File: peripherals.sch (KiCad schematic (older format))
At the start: 23 parts, among them IC5 ATECC608A-TNGLORAU-B, J4 Conn_Coaxial, SW1 KMR221NGLFS, SW2 KMR221NGLFS, U3 MAX-8Q, U4 BAT-HLD-001

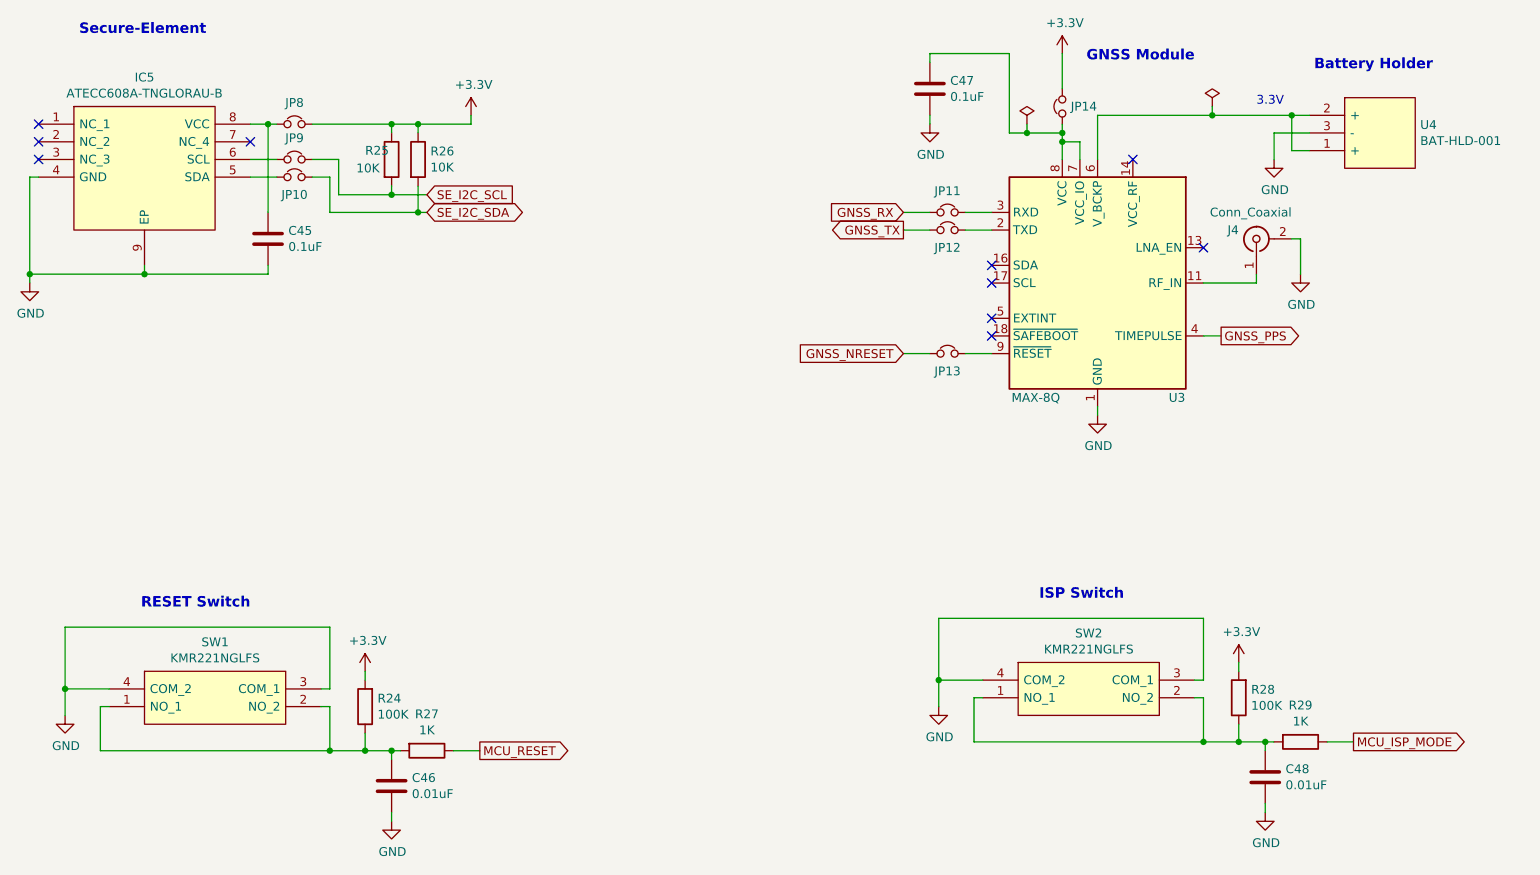
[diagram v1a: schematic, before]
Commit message: Removed jumpers from peripherals
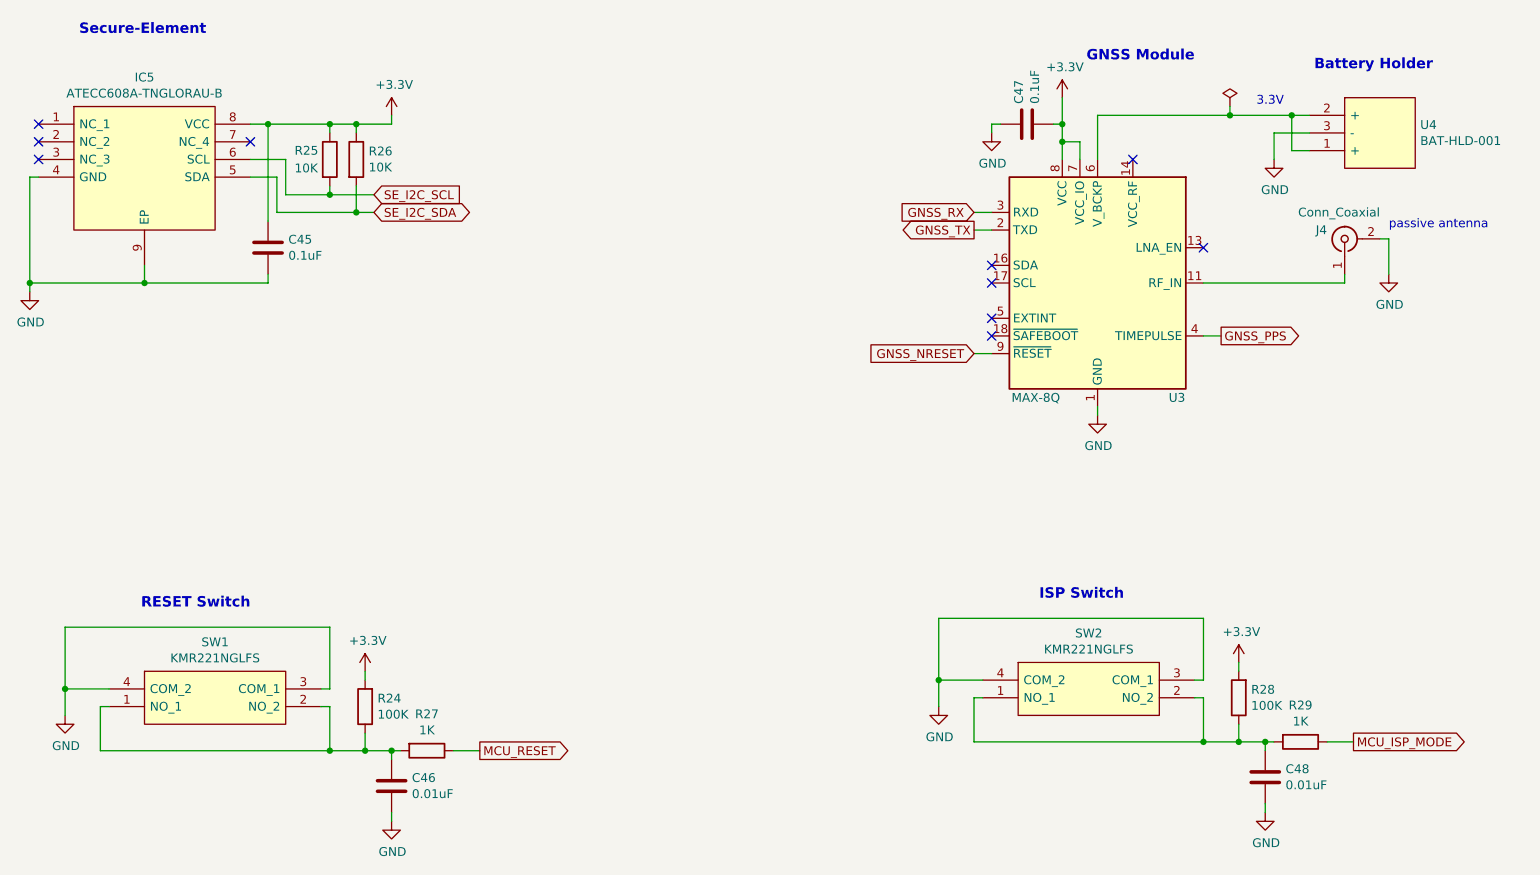
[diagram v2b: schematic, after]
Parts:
- removed JP10, JP11, JP12, JP13, JP14, JP8, JP9: Jumper_NC_Small, Jumper:SolderJumper-2_P1.3mm_Bridged_Pad1.0x1.5mm, symbol Device:Jumper_NC_Small
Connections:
- net +3V3: now also C45.1, C47.2, IC5.8 (VCC), U3.7 (VCC_IO), U3.8 (VCC)
- net GND: now also C47.1; no longer C47.2
- net GNSS_NRESET: now also U3.9 (~RESET)
- net GNSS_RX: now also U3.3 (RXD)
- net GNSS_TX: now also U3.2 (TXD)
- net SE_I2C_SCL: now also IC5.6 (SCL)
- net SE_I2C_SDA: now also IC5.5 (SDA)
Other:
- note added: "passive antenna"
- moved on the sheet: C45, C47, J4, R25, R26

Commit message: Changed all symbols names from IC to U
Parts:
- renumbered IC5 to U
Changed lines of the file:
@@
 P 2050 1900
 AR Path="/5F708DEE" Ref="IC?"  Part="1"
-AR Path="/5F708A6A/5F708DEE" Ref="IC5"  Part="1"
-F 0 "IC5" H 2650 2165 50  0000 C CNN
+AR Path="/5F708A6A/5F708DEE" Ref="U"  Part="1"
+F 0 "U" H 2650 2165 50  0000 C CNN
 F 1 "ATECC608A-TNGLORAU-B" H 2650 2074 50  0000 C CNN
 F 2 "tardigrade-components:SON50P300X200X60-9N" H 3100 2000 50  0001 L CNN

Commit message: Unnecessary note removed
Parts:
- renumbered U to U9
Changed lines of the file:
@@
 P 2050 1900
 AR Path="/5F708DEE" Ref="IC?"  Part="1"
-AR Path="/5F708A6A/5F708DEE" Ref="U"  Part="1"
-F 0 "U" H 2650 2165 50  0000 C CNN
+AR Path="/5F708A6A/5F708DEE" Ref="U9"  Part="1"
+F 0 "U9" H 2650 2165 50  0000 C CNN
 F 1 "ATECC608A-TNGLORAU-B" H 2650 2074 50  0000 C CNN
 F 2 "tardigrade-components:SON50P300X200X60-9N" H 3100 2000 50  0001 L CNN

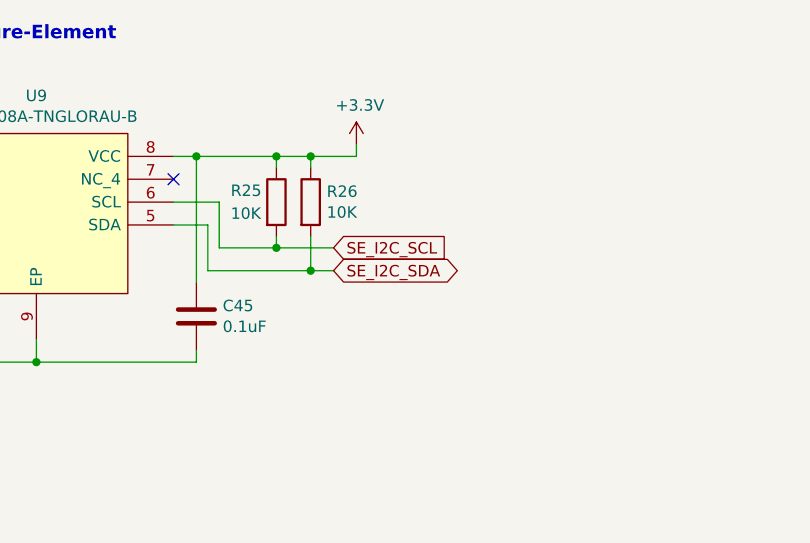
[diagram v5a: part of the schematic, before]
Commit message: Changed pin assignment on mcu and extension header
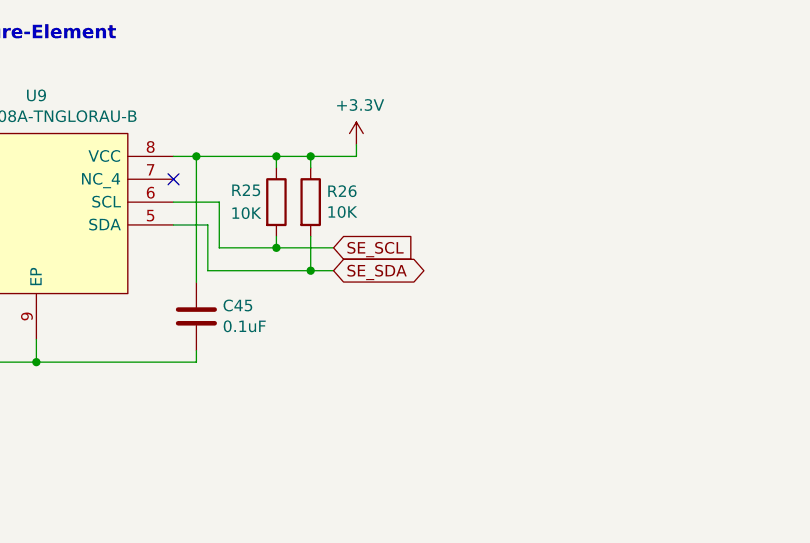
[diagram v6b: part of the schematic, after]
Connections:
- net SE_I2C_SCL renamed SE_SCL
- net SE_I2C_SDA renamed SE_SDA
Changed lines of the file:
@@
 	4050 1900 4050 1850
 Text GLabel 3950 2400 2    50   BiDi ~ 0
-SE_I2C_SDA
+SE_SDA
 Text GLabel 3950 2300 2    50   Input ~ 0
-SE_I2C_SCL
+SE_SCL
 $Comp
 L Device:C C45

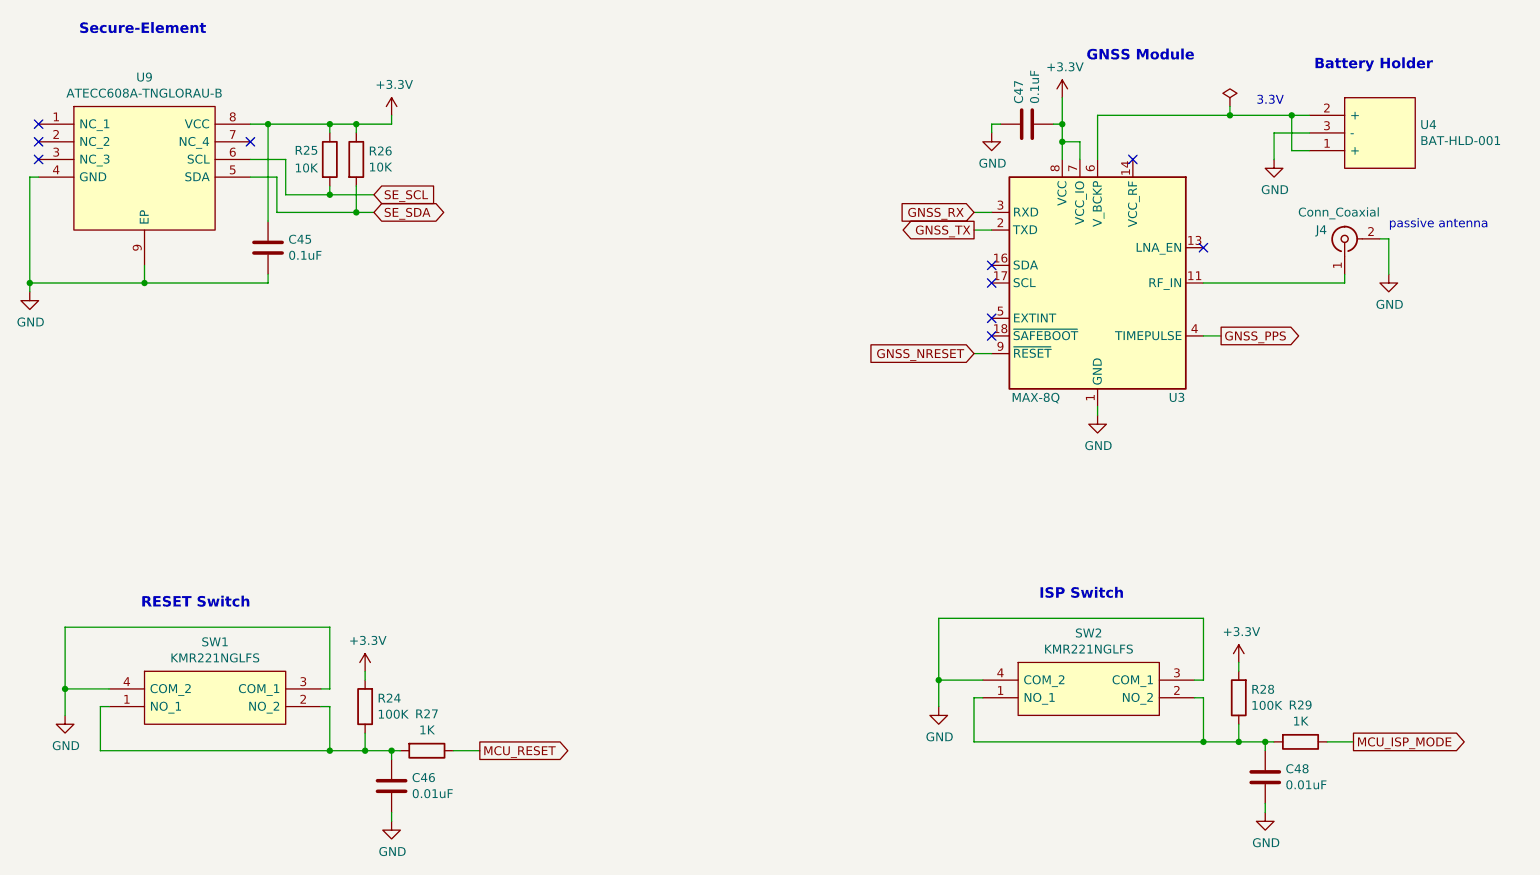
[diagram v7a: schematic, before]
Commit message: Major change of the layout (reviewed) for V1.1
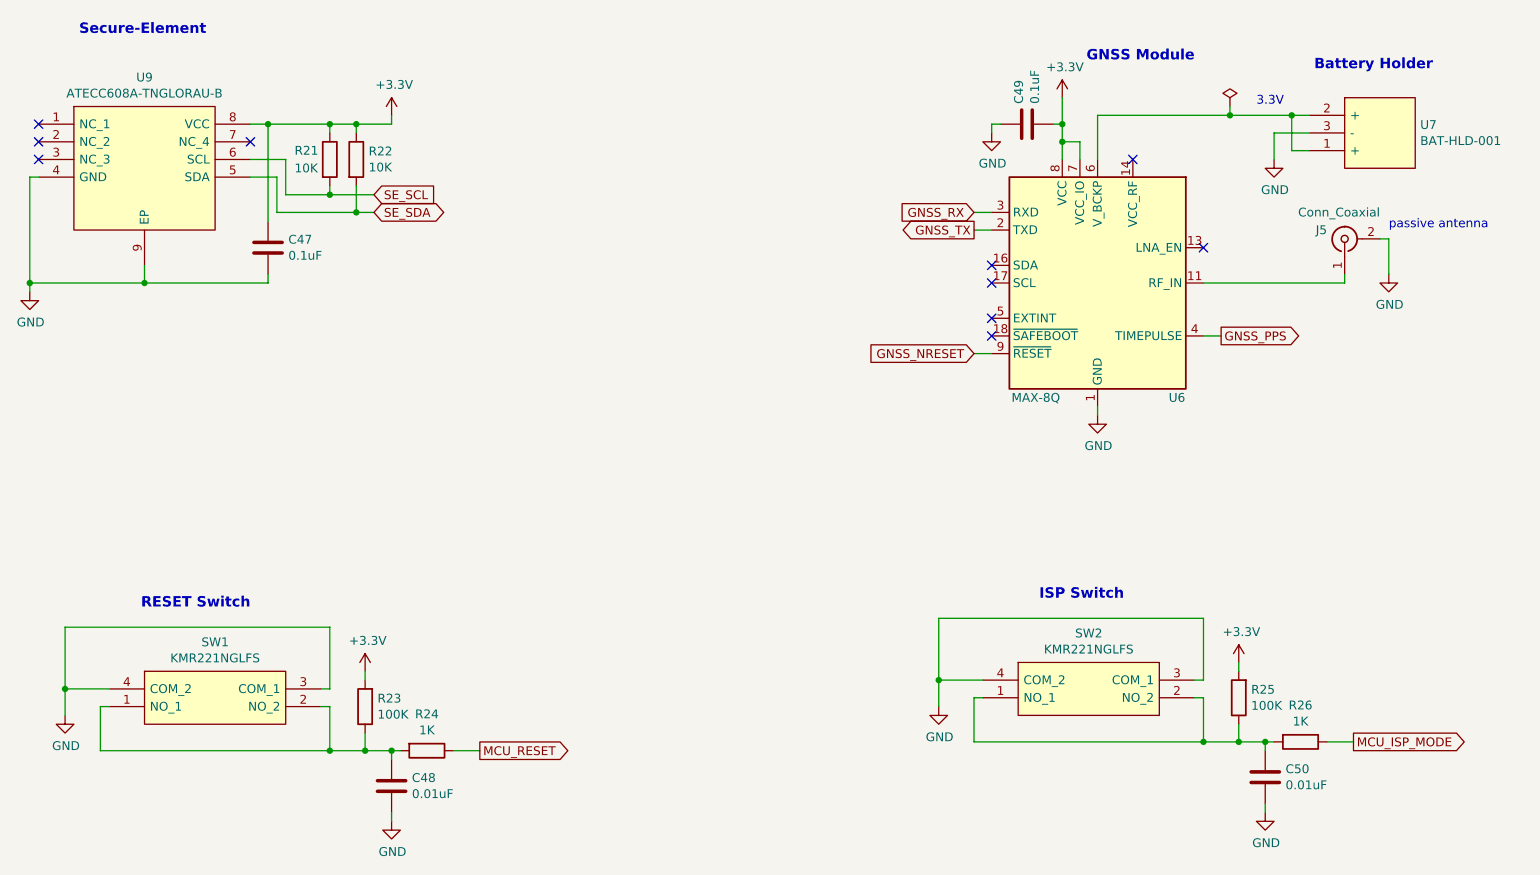
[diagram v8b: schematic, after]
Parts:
- renumbered C45 to C47, C46 to C48, C47 to C49, C48 to C50, J4 to J5, R25 to R21, R26 to R22, R24 to R23, R27 to R24, R28 to R25, R29 to R26, U3 to U6, U4 to U7
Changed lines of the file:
@@
 NoConn ~ 3250 2000
 $Comp
-L power:GND #PWR053
+L power:GND #PWR051
 U 1 1 5F709CF7
 P 2000 2850
-F 0 "#PWR053" H 2000 2600 50  0001 C CNN
+F 0 "#PWR051" H 2000 2600 50  0001 C CNN
 F 1 "GND" H 2005 2677 50  0000 C CNN
 F 2 "" H 2000 2850 50  0001 C CNN
@@
 	2000 2800 2000 2850
 $Comp
-L power:+3.3V #PWR057
+L power:+3.3V #PWR054
 U 1 1 5F70AC65
 P 4050 1850
-F 0 "#PWR057" H 4050 1700 50  0001 C CNN
+F 0 "#PWR054" H 4050 1700 50  0001 C CNN
 F 1 "+3.3V" H 4065 2023 50  0000 C CNN
 F 2 "" H 4050 1850 50  0001 C CNN
@@
 SE_SCL
 $Comp
-L Device:C C45
+L Device:C C47
 U 1 1 5F71C8D3
 P 3350 2600
-F 0 "C45" H 3465 2646 50  0000 L CNN
+F 0 "C47" H 3465 2646 50  0000 L CNN
 F 1 "0.1uF" H 3465 2555 50  0000 L CNN
 F 2 "Capacitor_SMD:C_0402_1005Metric" H 3388 2450 50  0001 C CNN
@@
 P 4050 5850
 AR Path="/5F6D82DD/5F87ACDE" Ref="#PWR?"  Part="1"
-AR Path="/5F708A6A/5F87ACDE" Ref="#PWR056"  Part="1"
-F 0 "#PWR056" H 4050 5600 50  0001 C CNN
+AR Path="/5F708A6A/5F87ACDE" Ref="#PWR055"  Part="1"
+F 0 "#PWR055" H 4050 5600 50  0001 C CNN
 F 1 "GND" H 4055 5677 50  0000 C CNN
 F 2 "" H 4050 5850 50  0001 C CNN
@@
 P 4250 5450
 AR Path="/5F6D82DD/5F87ACE4" Ref="R?"  Part="1"
-AR Path="/5F708A6A/5F87ACE4" Ref="R27"  Part="1"
-F 0 "R27" V 4043 5450 50  0000 C CNN
+AR Path="/5F708A6A/5F87ACE4" Ref="R24"  Part="1"
+F 0 "R24" V 4043 5450 50  0000 C CNN
 F 1 "1K" V 4134 5450 50  0000 C CNN
 F 2 "Resistor_SMD:R_0402_1005Metric" V 4180 5450 50  0001 C CNN
@@
 P 4050 5650
 AR Path="/5F6D82DD/5F87ACEB" Ref="C?"  Part="1"
-AR Path="/5F708A6A/5F87ACEB" Ref="C46"  Part="1"
-F 0 "C46" H 4165 5696 50  0000 L CNN
+AR Path="/5F708A6A/5F87ACEB" Ref="C48"  Part="1"
+F 0 "C48" H 4165 5696 50  0000 L CNN
 F 1 "0.01uF" H 4165 5605 50  0000 L CNN
 F 2 "Capacitor_SMD:C_0402_1005Metric" H 4088 5500 50  0001 C CNN
@@
 P 2200 5250
 AR Path="/5F6D82DD/5F87AD0C" Ref="#PWR?"  Part="1"
-AR Path="/5F708A6A/5F87AD0C" Ref="#PWR054"  Part="1"
-F 0 "#PWR054" H 2200 5000 50  0001 C CNN
+AR Path="/5F708A6A/5F87AD0C" Ref="#PWR052"  Part="1"
+F 0 "#PWR052" H 2200 5000 50  0001 C CNN
 F 1 "GND" H 2205 5077 50  0000 C CNN
 F 2 "" H 2200 5250 50  0001 C CNN
@@
 P 3900 5200
 AR Path="/5F6D82DD/5FAB25E7" Ref="R?"  Part="1"
-AR Path="/5F708A6A/5FAB25E7" Ref="R24"  Part="1"
-F 0 "R24" H 3830 5154 50  0000 R CNN
+AR Path="/5F708A6A/5FAB25E7" Ref="R23"  Part="1"
+F 0 "R23" H 3830 5154 50  0000 R CNN
 F 1 "100K" H 3830 5245 50  0000 R CNN
 F 2 "Resistor_SMD:R_0402_1005Metric" V 3830 5200 50  0001 C CNN
@@
 P 9000 5800
 AR Path="/5F6D82DD/5FABF160" Ref="#PWR?"  Part="1"
-AR Path="/5F708A6A/5FABF160" Ref="#PWR063"  Part="1"
-F 0 "#PWR063" H 9000 5550 50  0001 C CNN
+AR Path="/5F708A6A/5FABF160" Ref="#PWR061"  Part="1"
+F 0 "#PWR061" H 9000 5550 50  0001 C CNN
 F 1 "GND" H 9005 5627 50  0000 C CNN
 F 2 "" H 9000 5800 50  0001 C CNN
@@
 P 9200 5400
 AR Path="/5F6D82DD/5FABF166" Ref="R?"  Part="1"
-AR Path="/5F708A6A/5FABF166" Ref="R29"  Part="1"
-F 0 "R29" V 8993 5400 50  0000 C CNN
+AR Path="/5F708A6A/5FABF166" Ref="R26"  Part="1"
+F 0 "R26" V 8993 5400 50  0000 C CNN
 F 1 "1K" V 9084 5400 50  0000 C CNN
 F 2 "Resistor_SMD:R_0402_1005Metric" V 9130 5400 50  0001 C CNN
@@
 P 9000 5600
 AR Path="/5F6D82DD/5FABF16D" Ref="C?"  Part="1"
-AR Path="/5F708A6A/5FABF16D" Ref="C48"  Part="1"
-F 0 "C48" H 9115 5646 50  0000 L CNN
+AR Path="/5F708A6A/5FABF16D" Ref="C50"  Part="1"
+F 0 "C50" H 9115 5646 50  0000 L CNN
 F 1 "0.01uF" H 9115 5555 50  0000 L CNN
 F 2 "Capacitor_SMD:C_0402_1005Metric" H 9038 5450 50  0001 C CNN
@@
 P 7150 5200
 AR Path="/5F6D82DD/5FABF188" Ref="#PWR?"  Part="1"
-AR Path="/5F708A6A/5FABF188" Ref="#PWR059"  Part="1"
-F 0 "#PWR059" H 7150 4950 50  0001 C CNN
+AR Path="/5F708A6A/5FABF188" Ref="#PWR056"  Part="1"
+F 0 "#PWR056" H 7150 4950 50  0001 C CNN
 F 1 "GND" H 7155 5027 50  0000 C CNN
 F 2 "" H 7150 5200 50  0001 C CNN
@@
 P 8850 5150
 AR Path="/5F6D82DD/5FABF1A3" Ref="R?"  Part="1"
-AR Path="/5F708A6A/5FABF1A3" Ref="R28"  Part="1"
-F 0 "R28" H 8780 5104 50  0000 R CNN
+AR Path="/5F708A6A/5FABF1A3" Ref="R25"  Part="1"
+F 0 "R25" H 8780 5104 50  0000 R CNN
 F 1 "100K" H 8780 5195 50  0000 R CNN
 F 2 "Resistor_SMD:R_0402_1005Metric" V 8780 5150 50  0001 C CNN
@@
 	8850 5300 8850 5400
 $Comp
-L Device:R R26
+L Device:R R22
 U 1 1 5F76B902
 P 3850 2100
-F 0 "R26" H 3920 2146 50  0000 L CNN
+F 0 "R22" H 3920 2146 50  0000 L CNN
 F 1 "10K" H 3920 2055 50  0000 L CNN
 F 2 "Resistor_SMD:R_0402_1005Metric" V 3780 2100 50  0001 C CNN
@@
 	3850 2400 3950 2400
 $Comp
-L power:GND #PWR064
+L power:GND #PWR062
 U 1 1 5F7B513C
 P 9050 2100
-F 0 "#PWR064" H 9050 1850 50  0001 C CNN
+F 0 "#PWR062" H 9050 1850 50  0001 C CNN
 F 1 "GND" H 9055 1927 50  0000 C CNN
 F 2 "" H 9050 2100 50  0001 C CNN
@@
 Battery Holder
 $Comp
-L tardigrade-components:BAT-HLD-001 U4
+L tardigrade-components:BAT-HLD-001 U7
 U 1 1 5F7B443C
 P 9250 1850
-F 0 "U4" H 9878 1796 50  0000 L CNN
+F 0 "U7" H 9878 1796 50  0000 L CNN
 F 1 "BAT-HLD-001" H 9878 1705 50  0000 L CNN
 F 2 "tardigrade-components:BATHLD001" H 9900 1950 50  0001 L CNN
@@
 Connection ~ 9150 1850
 $Comp
-L Device:R R25
+L Device:R R21
 U 1 1 5F76B3C5
 P 3700 2100
-F 0 "R25" H 3500 2150 50  0000 L CNN
+F 0 "R21" H 3500 2150 50  0000 L CNN
 F 1 "10K" H 3500 2050 50  0000 L CNN
 F 2 "Resistor_SMD:R_0402_1005Metric" V 3630 2100 50  0001 C CNN
@@
 $EndComp
 $Comp
-L power:+3.3V #PWR055
+L power:+3.3V #PWR053
 U 1 1 5F82B908
 P 3900 5000
-F 0 "#PWR055" H 3900 4850 50  0001 C CNN
+F 0 "#PWR053" H 3900 4850 50  0001 C CNN
 F 1 "+3.3V" H 3915 5173 50  0000 C CNN
 F 2 "" H 3900 5000 50  0001 C CNN
@@
 $EndComp
 $Comp
-L power:+3.3V #PWR062
+L power:+3.3V #PWR060
 U 1 1 5F82BE1A
 P 8850 4950
-F 0 "#PWR062" H 8850 4800 50  0001 C CNN
+F 0 "#PWR060" H 8850 4800 50  0001 C CNN
 F 1 "+3.3V" H 8865 5123 50  0000 C CNN
 F 2 "" H 8850 4950 50  0001 C CNN
@@
 3.3V
 $Comp
-L RF_GPS:MAX-8Q U3
+L RF_GPS:MAX-8Q U6
 U 1 1 5F8800F1
 P 8050 2800
-F 0 "U3" H 8500 2150 50  0000 C CNN
+F 0 "U6" H 8500 2150 50  0000 C CNN
 F 1 "MAX-8Q" H 7700 2150 50  0000 C CNN
 F 2 "RF_GPS:ublox_MAX" H 8450 2150 50  0001 C CNN
@@
 	7950 2100 7950 2000
 $Comp
-L power:+3.3V #PWR060
+L power:+3.3V #PWR058
 U 1 1 5F897B8E
 P 7850 1750
-F 0 "#PWR060" H 7850 1600 50  0001 C CNN
+F 0 "#PWR058" H 7850 1600 50  0001 C CNN
 F 1 "+3.3V" H 7865 1923 50  0000 C CNN
 F 2 "" H 7850 1750 50  0001 C CNN
@@
 $EndComp
 $Comp
-L Connector:Conn_Coaxial J4
+L Connector:Conn_Coaxial J5
 U 1 1 5F8A9081
 P 9450 2550
-F 0 "J4" V 9500 2650 50  0000 L CNN
+F 0 "J5" V 9500 2650 50  0000 L CNN
 F 1 "Conn_Coaxial" V 9600 2350 50  0000 L CNN
 F 2 "Connector_Coaxial:U.FL_Hirose_U.FL-R-SMT-1_Vertical" H 9450 2550 50  0001 C CNN
@@
 	8750 3100 8650 3100
 $Comp
-L Device:C C47
+L Device:C C49
 U 1 1 5F8BC520
 P 7650 1900
-F 0 "C47" H 7765 1946 50  0000 L CNN
+F 0 "C49" H 7765 1946 50  0000 L CNN
 F 1 "0.1uF" H 7765 1855 50  0000 L CNN
 F 2 "Capacitor_SMD:C_0402_1005Metric" H 7688 1750 50  0001 C CNN
@@
 $EndComp
 $Comp
-L power:GND #PWR058
+L power:GND #PWR057
 U 1 1 5F8BD72B
 P 7450 1950
-F 0 "#PWR058" H 7450 1700 50  0001 C CNN
+F 0 "#PWR057" H 7450 1700 50  0001 C CNN
 F 1 "GND" H 7455 1777 50  0000 C CNN
 F 2 "" H 7450 1950 50  0001 C CNN
@@
 	7850 2000 7850 2100
 $Comp
-L power:GND #PWR061
+L power:GND #PWR059
 U 1 1 5F938540
 P 8050 3550
-F 0 "#PWR061" H 8050 3300 50  0001 C CNN
+F 0 "#PWR059" H 8050 3300 50  0001 C CNN
 F 1 "GND" H 8055 3377 50  0000 C CNN
 F 2 "" H 8050 3550 50  0001 C CNN
@@
 	9700 2550 9700 2750
 $Comp
-L power:GND #PWR0107
+L power:GND #PWR063
 U 1 1 5FACD002
 P 9700 2750
-F 0 "#PWR0107" H 9700 2500 50  0001 C CNN
+F 0 "#PWR063" H 9700 2500 50  0001 C CNN
 F 1 "GND" H 9705 2577 50  0000 C CNN
 F 2 "" H 9700 2750 50  0001 C CNN
@@
 $EndComp
 $Comp
-L power:PWR_FLAG #FLG0101
+L power:PWR_FLAG #FLG05
 U 1 1 5FACFF74
 P 8800 1800
-F 0 "#FLG0101" H 8800 1875 50  0001 C CNN
+F 0 "#FLG05" H 8800 1875 50  0001 C CNN
 F 1 "PWR_FLAG" H 8800 1973 50  0001 C CNN
 F 2 "" H 8800 1800 50  0001 C CNN
